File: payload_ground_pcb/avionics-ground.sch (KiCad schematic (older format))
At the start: 14 parts

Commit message: Work on ground station and new IMU added to payload
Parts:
- added J1: Micro_SD_Card, Connector_Card:microSD_HC_Wuerth_693072010801, symbol Connector:Micro_SD_Card
- added J2: Conn_Coaxial, Connector_Coaxial:SMA_Amphenol_132134-14_Vertical, symbol Connector:Conn_Coaxial
- added J?: USB_B_Micro, symbol Connector:USB_B_Micro
- added M1, M2: Stepper_Motor_bipolar, symbol Motor:Stepper_Motor_bipolar
- added R1: R, symbol Device:R
- added SW1: SW_Push, Button_Switch_THT:SW_PUSH_6mm, symbol Switch:SW_Push
- added U2: RFM95W-915S2, RF_Module:HOPERF_RFM9XW_SMD, symbol RF_Module:RFM95W-915S2
- added U?: ublox_SAM-M8Q, RF_GPS:ublox_SAM-M8Q, symbol RF_GPS:ublox_SAM-M8Q
- gave numbers to parts that had none: 14
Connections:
- net +3V3: now also U1.16 (3V3), U2.13 (3.3V)
- net Audio: now also U1.28 (21_A7_RX5_BCLK1)
- net DB0: now also U1.5 (3_LRCLK2)
- net DB1: now also U1.6 (4_BCLK2)
- net DB2: now also U1.7 (5_IN2)
- net DB3: now also U1.8 (6_OUT1D)
- net DB4: now also U1.22 (15_A1_RX3_SPDIF_IN)
- net DB5: now also U1.23 (16_A2_RX4_SCL1)
- net DB6: now also U1.24 (17_A3_TX4_SDA1)
- net DB7: now also U1.25 (18_A4_SDA0)
- net E: now also U1.4 (2_OUT2)
- net GND: now also U1.1 (GND), U1.17 (GND), U1.32 (GND), J2.2 (Ext), R1.2, SW1.1, U2.1 (GND), U2.10 (GND), U2.8 (GND)
- net RS: now also U1.2 (0_RX1_CRX2_CS1)
- net RW: now also U1.3 (1_TX1_CTX2_MISO1)
- net CS: now reaches U1.12 (10_CS_MQSR)
- net CS: now also R1.1, U2.5 (NSS)
- net MOSI: now reaches U1.13 (11_MOSI_CTX1)
- net MOSI: now also U2.3 (MOSI)
- net MISO: now reaches U1.14 (12_MISO_MQSL)
- net MISO: now also U2.2 (MISO)
- net SCK: now reaches U1.20 (13_SCK_CRX1_LED)
- net SCK: now also U2.4 (SCK)
- net DAT1: now reaches U1.45 (34_DAT1_MISO2)
- net DAT1: now also J1.8 (DAT1)
- net DAT0: now reaches U1.46 (35_DAT0_MOSI2)
- net DAT0: now also J1.7 (DAT0)
- net VSS: now reaches U1.47 (GND)
- net VSS: now also J1.6 (VSS)
- net CLK: now reaches U1.48 (36_CLK_CS2)
- net CLK: now also J1.5 (CLK)
- net VDD: now reaches U1.49 (3V3)
- net VDD: now also J1.4 (VDD)
- net CMD: now reaches U1.50 (37_CMD_SCK2)
- net CMD: now also J1.3 (CMD)
- net DAT3: now reaches U1.51 (38_DAT3_RX5)
- net DAT3: now also J1.2 (DAT3/CD)
- net DAT2: now reaches U1.52 (39_DAT2_TX5)
- net DAT2: now also J1.1 (DAT2)
- new net: SW1.2, U2.6 (RESET)
- new net: J2.1 (In), U2.9 (ANT)
- new net: U?.1 (GND), U?.10 (GND), U?.11 (GND), U?.15 (GND), U?.16 (GND), U?.20 (GND), U?.4 (GND), U?.5 (GND), U?.6 (GND)
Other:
- note added: "1"
- note added: "1\n"
- note added: "A\n"
- note added: "Ground Station PCB"
- note added: "October 2019\n"
- moved on the sheet: RV1, U3

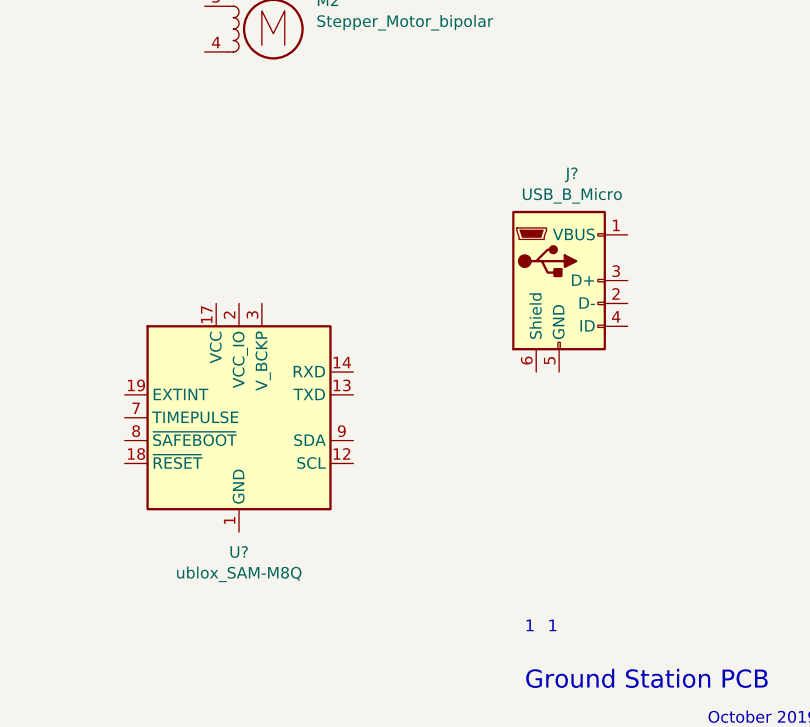
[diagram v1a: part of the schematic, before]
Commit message: Wired boards using autorouter
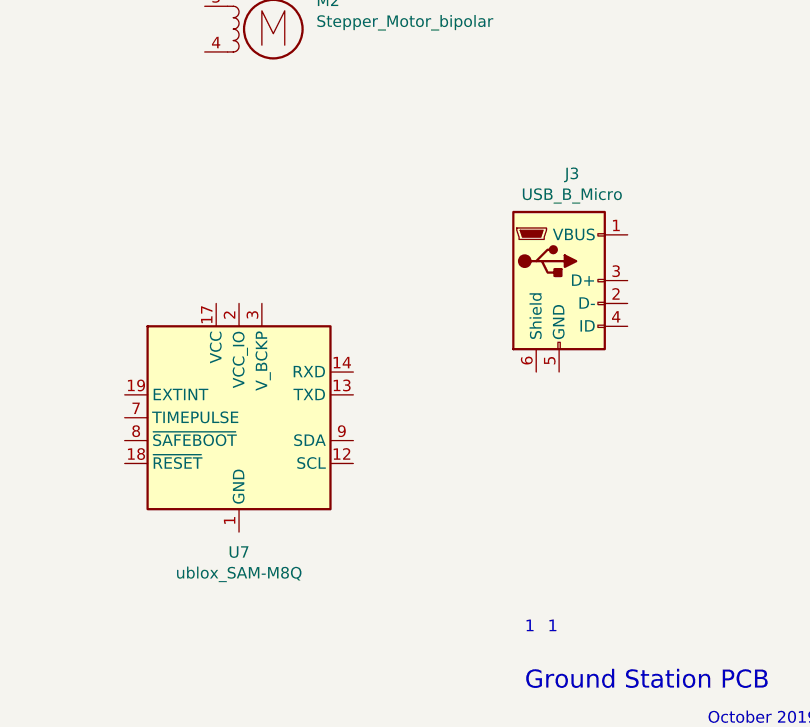
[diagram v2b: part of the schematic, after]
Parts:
- C1, C2, C3, C4: footprint (none) -> Capacitor_Tantalum_SMD:CP_EIA-1608-08_AVX-J_Pad1.25x1.05mm_HandSolder
- J3: renamed from J?; footprint (none) -> Connector_USB:USB_Mini-B_Lumberg_2486_01_Horizontal
- LS1: footprint (none) -> Buzzer_Beeper:Buzzer_Murata_PKMCS0909E4000-R1
- R1, R2, R3: footprint (none) -> Resistor_SMD:R_0805_2012Metric_Pad1.15x1.40mm_HandSolder
- RV1, RV2: footprint (none) -> Potentiometer_SMD:Potentiometer_ACP_CA6-VSMD_Vertical_Hole
- U1: footprint (none) -> footprints:Teensy40
- U4: footprint (none) -> Package_DIP:DIP-8_W7.62mm_SMDSocket_SmallPads
- gave numbers to parts that had none: 1
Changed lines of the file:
@@
 F 0 "U1" H 2350 4165 50  0000 C CNN
 F 1 "Teensy4.0" H 2350 4074 50  0000 C CNN
-F 2 "" H 1950 2750 50  0001 C CNN
+F 2 "footprints:Teensy40" H 1950 2750 50  0001 C CNN
 F 3 "" H 1950 2750 50  0001 C CNN
 	1    2350 2550
@@
 F 0 "C4" H 9865 5446 50  0000 L CNN
 F 1 "3.3uF" H 9865 5355 50  0000 L CNN
-F 2 "" H 9750 5400 50  0001 C CNN
+F 2 "Capacitor_Tantalum_SMD:CP_EIA-1608-08_AVX-J_Pad1.25x1.05mm_HandSolder" H 9750 5400 50  0001 C CNN
 F 3 "~" H 9750 5400 50  0001 C CNN
 	1    9750 5400
@@
 F 0 "RV2" H 8681 2096 50  0000 R CNN
 F 1 "R_POT" H 8681 2005 50  0000 R CNN
-F 2 "" H 8750 2050 50  0001 C CNN
+F 2 "Potentiometer_SMD:Potentiometer_ACP_CA6-VSMD_Vertical_Hole" H 8750 2050 50  0001 C CNN
 F 3 "~" H 8750 2050 50  0001 C CNN
 	1    8750 2050
@@
 F 0 "C3" H 9865 4496 50  0000 L CNN
 F 1 "3.3uF" H 9865 4405 50  0000 L CNN
-F 2 "" H 9750 4450 50  0001 C CNN
+F 2 "Capacitor_Tantalum_SMD:CP_EIA-1608-08_AVX-J_Pad1.25x1.05mm_HandSolder" H 9750 4450 50  0001 C CNN
 F 3 "~" H 9750 4450 50  0001 C CNN
 	1    9750 4450
@@
 F 0 "R2" V 8693 1350 50  0000 C CNN
 F 1 "R" V 8784 1350 50  0000 C CNN
-F 2 "" V 8830 1350 50  0001 C CNN
+F 2 "Resistor_SMD:R_0805_2012Metric_Pad1.15x1.40mm_HandSolder" V 8830 1350 50  0001 C CNN
 F 3 "~" H 8900 1350 50  0001 C CNN
 	1    8900 1350
@@
 F 0 "C1" H 9009 1454 50  0000 R CNN
 F 1 "CP1_Small" H 9009 1545 50  0000 R CNN
-F 2 "" H 9100 1500 50  0001 C CNN
+F 2 "Capacitor_Tantalum_SMD:CP_EIA-1608-08_AVX-J_Pad1.25x1.05mm_HandSolder" H 9100 1500 50  0001 C CNN
 F 3 "~" H 9100 1500 50  0001 C CNN
 	1    9100 1500
@@
 F 0 "R3" H 9231 2804 50  0000 R CNN
 F 1 "R" H 9231 2895 50  0000 R CNN
-F 2 "" V 9230 2850 50  0001 C CNN
+F 2 "Resistor_SMD:R_0805_2012Metric_Pad1.15x1.40mm_HandSolder" V 9230 2850 50  0001 C CNN
 F 3 "~" H 9300 2850 50  0001 C CNN
 	1    9300 2850
@@
 F 0 "C2" H 9491 2646 50  0000 L CNN
 F 1 "CP1_Small" H 9491 2555 50  0000 L CNN
-F 2 "" H 9400 2600 50  0001 C CNN
+F 2 "Capacitor_Tantalum_SMD:CP_EIA-1608-08_AVX-J_Pad1.25x1.05mm_HandSolder" H 9400 2600 50  0001 C CNN
 F 3 "~" H 9400 2600 50  0001 C CNN
 	1    9400 2600
@@
 F 0 "U4" H 9644 2196 50  0000 L CNN
 F 1 "LM386" H 9644 2105 50  0000 L CNN
-F 2 "" H 9400 2250 50  0001 C CNN
+F 2 "Package_DIP:DIP-8_W7.62mm_SMDSocket_SmallPads" H 9400 2250 50  0001 C CNN
 F 3 "http://www.ti.com/lit/ds/symlink/lm386.pdf" H 9500 2350 50  0001 C CNN
 	1    9300 2150
@@
 F 0 "LS1" H 10270 1746 50  0000 L CNN
 F 1 "Speaker" H 10270 1655 50  0000 L CNN
-F 2 "" H 10100 1550 50  0001 C CNN
+F 2 "Buzzer_Beeper:Buzzer_Murata_PKMCS0909E4000-R1" H 10100 1550 50  0001 C CNN
 F 3 "~" H 10090 1700 50  0001 C CNN
 	1    10100 1750
@@
 F 0 "R1" V 5143 1650 50  0000 C CNN
 F 1 "R" V 5234 1650 50  0000 C CNN
-F 2 "" V 5280 1650 50  0001 C CNN
+F 2 "Resistor_SMD:R_0805_2012Metric_Pad1.15x1.40mm_HandSolder" V 5280 1650 50  0001 C CNN
 F 3 "~" H 5350 1650 50  0001 C CNN
 	1    5350 1650
@@
 F 0 "RV1" H 4431 4946 50  0000 R CNN
 F 1 "R_POT" H 4431 4855 50  0000 R CNN
-F 2 "" H 4500 4900 50  0001 C CNN
+F 2 "Potentiometer_SMD:Potentiometer_ACP_CA6-VSMD_Vertical_Hole" H 4500 4900 50  0001 C CNN
 F 3 "~" H 4500 4900 50  0001 C CNN
 	1    4500 4900
@@
 	3650 6500 3700 6500
 $Comp
-L RF_GPS:ublox_SAM-M8Q U?
+L RF_GPS:ublox_SAM-M8Q U7
 U 1 1 5DA664A7
 P 6050 6300
-F 0 "U?" H 6050 5711 50  0000 C CNN
+F 0 "U7" H 6050 5711 50  0000 C CNN
 F 1 "ublox_SAM-M8Q" H 6050 5620 50  0000 C CNN
 F 2 "RF_GPS:ublox_SAM-M8Q" H 6550 5850 50  0001 C CNN
@@
 $EndComp
 $Comp
-L Connector:USB_B_Micro J?
+L Connector:USB_B_Micro J3
 U 1 1 5DA6D7F2
 P 7450 5700
-F 0 "J?" H 7507 6167 50  0000 C CNN
+F 0 "J3" H 7507 6167 50  0000 C CNN
 F 1 "USB_B_Micro" H 7507 6076 50  0000 C CNN
-F 2 "" H 7600 5650 50  0001 C CNN
+F 2 "Connector_USB:USB_Mini-B_Lumberg_2486_01_Horizontal" H 7600 5650 50  0001 C CNN
 F 3 "~" H 7600 5650 50  0001 C CNN
 	1    7450 5700

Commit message: REV B
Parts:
- removed C1, C2: CP1_Small, Capacitor_Tantalum_SMD:CP_EIA-1608-08_AVX-J_Pad1.25x1.05mm_HandSolder, symbol Device:CP1_Small
- removed J3: USB_B_Micro, Connector_USB:USB_Mini-B_Lumberg_2486_01_Horizontal, symbol Connector:USB_B_Micro
- removed LS1: Speaker, Buzzer_Beeper:Buzzer_Murata_PKMCS0909E4000-R1, symbol Device:Speaker
- removed R2, R3: R, Resistor_SMD:R_0805_2012Metric_Pad1.15x1.40mm_HandSolder, symbol Device:R
- removed RV2: R_POT, Potentiometer_SMD:Potentiometer_ACP_CA6-VSMD_Vertical_Hole, symbol Device:R_POT
- removed U4: LM386, Package_DIP:DIP-8_W7.62mm_SMDSocket_SmallPads, symbol Amplifier_Audio:LM386
- added J?: USB_C_Receptacle_USB2.0, symbol Connector:USB_C_Receptacle_USB2.0
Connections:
- net +5V: now also U6.1 (VI)
- net +BATT: no longer U6.1 (VI)
- net GND: now also J?.A1 (GND), J?.A12 (GND), J?.B1 (GND), J?.B12 (GND), J?.S1 (SHIELD)
- new net: J?.A4 (VBUS), J?.A9 (VBUS), J?.B4 (VBUS), J?.B9 (VBUS)
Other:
- note removed: "Audio\n"
- moved on the sheet: C3, M1, U5
